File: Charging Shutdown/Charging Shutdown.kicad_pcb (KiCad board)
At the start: 2 copper layers, 52.3 x 56 mm, 15 parts, among them J2 776280-1, K1 V23047A1012A511, K3 V23047A1012A511, Q1 2N2222, Q3 2N2222

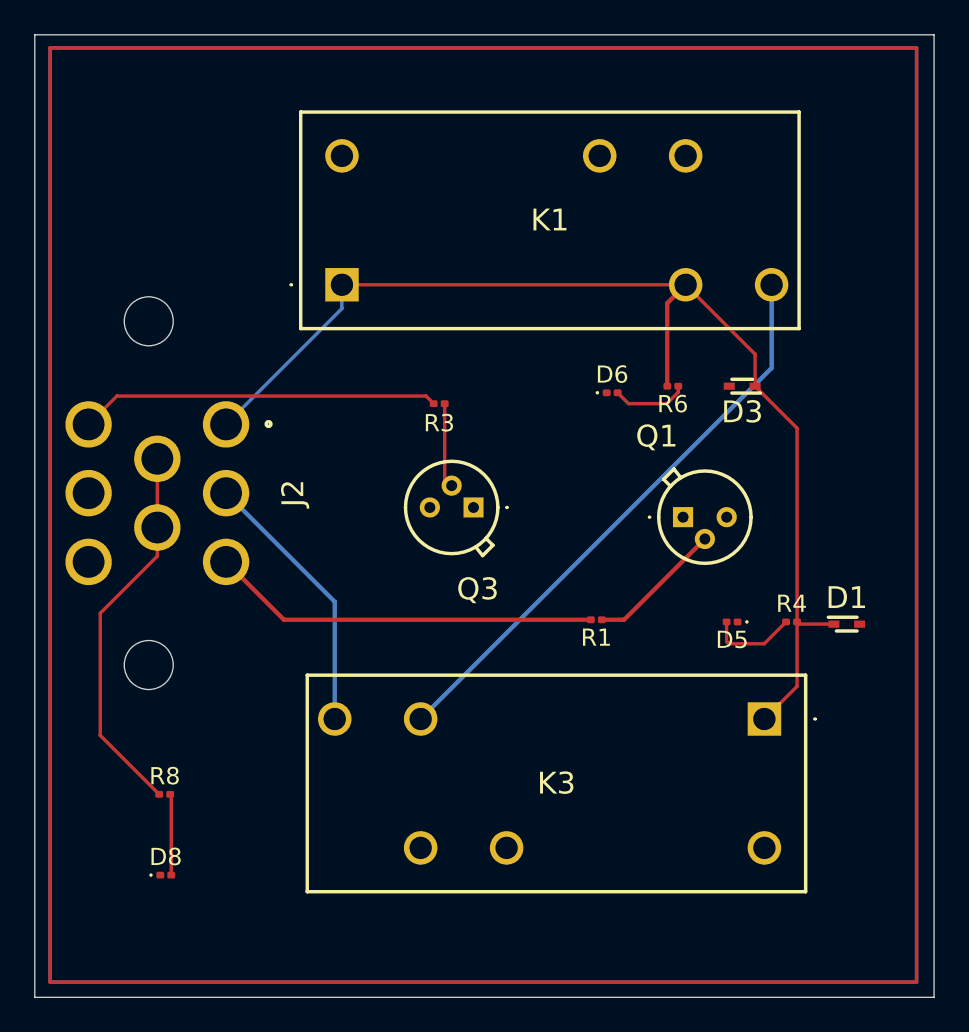
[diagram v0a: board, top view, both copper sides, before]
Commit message: BSPD, Shutdown/Charging Shutdown, & Voltage Indicator final changes
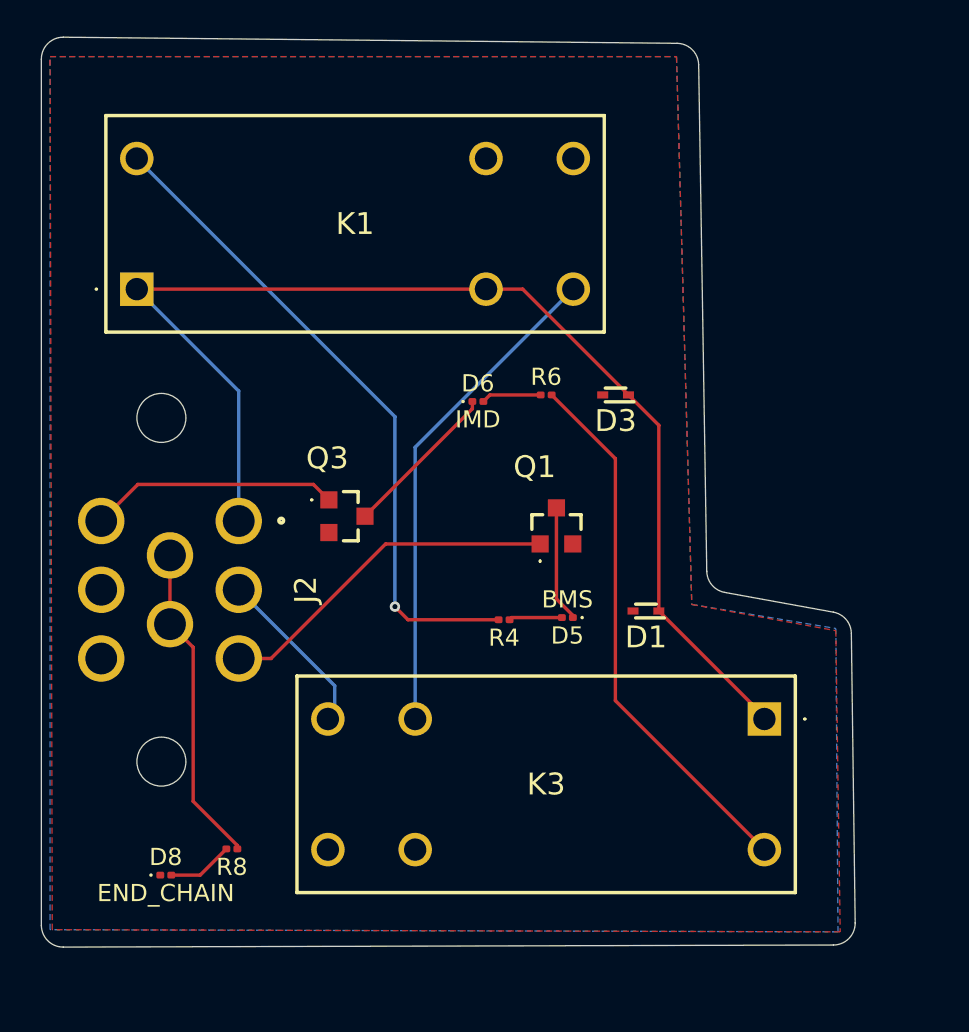
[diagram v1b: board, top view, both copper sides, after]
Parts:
- removed R1, R3: 680, Resistor_SMD:R_0201_0603Metric
- K1, K3: value V23047A1012A511 -> PR2212V4001A; footprint SDM_MiscFootprint:V23047A1012A511 -> Shutdown_Footprint:PR2212V4001A
- Q1, Q3: footprint Shutdown_Footprint:2N2222 -> Shutdown_Footprint:ZXM61N02FTC
- moved R4 16.7 mm to (108.5, 98.8), turned to 180 degrees
- moved K1 11.9 mm to (87.1, 79.6)
- moved D1 11.7 mm to (116.7, 98.3), turned to 180 degrees
- moved D5 9.59 mm to (112.1, 98.7)
- moved D6 7.83 mm to (106.9, 86.1)
- moved Q3 7.38 mm to (99.3, 92.8), turned to -90 degrees
- moved D3 7.38 mm to (114.9, 85.7)
- moved Q1 7.38 mm to (111.5, 93.3)
- moved R6 7.38 mm to (110.9, 85.7), turned to 0 degrees
- moved J2 5.67 mm to (77.2, 97.1)
- moved R8 5.03 mm to (92.6, 112.1), turned to 180 degrees
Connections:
- D5 pad 1: GND -> Net-(D5-K)
- D6 pad 1: GND -> Net-(D6-K)
- K1 pad 2: GND -> +12V
- K3 pad 2: GND -> Net-(K1-NO_1)
- Q1 pad 1: GND -> /BMS KILL SIGNAL
- Q1 pad 2: Net-(Q1-B) -> Net-(D5-K)
- Q3 pad 1: GND -> /IMD KILL SIGNAL
- Q3 pad 2: Net-(Q3-B) -> Net-(D6-K)
- R4 pad 2: +12V -> Net-(K1-COIL_2)
- R6 pad 2: +12V -> Net-(K3-COM_1)
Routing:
- net Net-(K1-COIL_2): track 0.00 -> 38.6 mm, vias 0 -> 1
- net Net-(K3-COM_1): track 0.00 -> 31.6 mm
- net Net-(D6-K): track 0.00 -> 9.26 mm
- net Net-(Q1-B): track 7.94 -> 0.00 mm
- net Net-(D5-K): track 0.00 -> 6.78 mm
- net /IMD KILL SIGNAL: track 20.9 -> 14.5 mm
- net /RELAYS_OUT: track 15.8 -> 9.83 mm
- net Net-(Q3-B): track 4.94 -> 0.00 mm
- net Net-(K1-NO_1): track 33.7 -> 28.8 mm
- net Shutdown Signal: track 22.3 -> 18.7 mm
- net /BMS KILL SIGNAL: track 22.6 -> 20.3 mm
- net Net-(D5-A): track 5.18 -> 3.10 mm
- net Net-(D6-A): track 4.42 -> 3.49 mm
- net Net-(D8-A): track 4.72 -> 3.84 mm
- net +12V: track 68.2 -> 68.9 mm
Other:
- board size 52.3 x 56 mm -> 47.4 x 52.9 mm
